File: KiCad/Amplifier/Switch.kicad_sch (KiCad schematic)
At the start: 49 parts, among them Q1 BD139, Q2 IXTH90P10P, Q4 BD139, Q5A1 BSC340N08NS3G, Q6 BD139, U1 AD8033

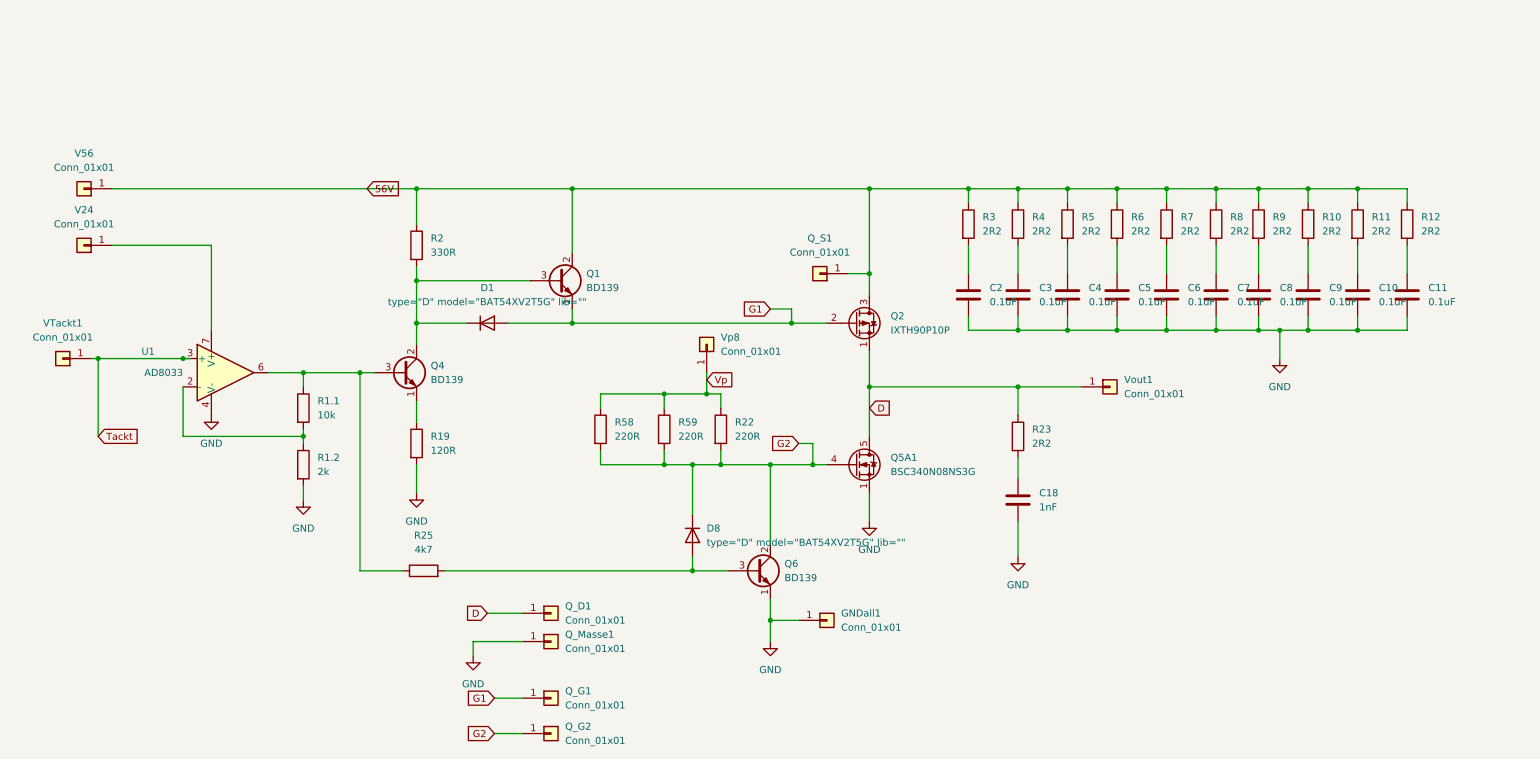
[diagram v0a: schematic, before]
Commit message: update Ampilfier
Schematic updated with separate pages.
all footprints added.
to do :
HF Part
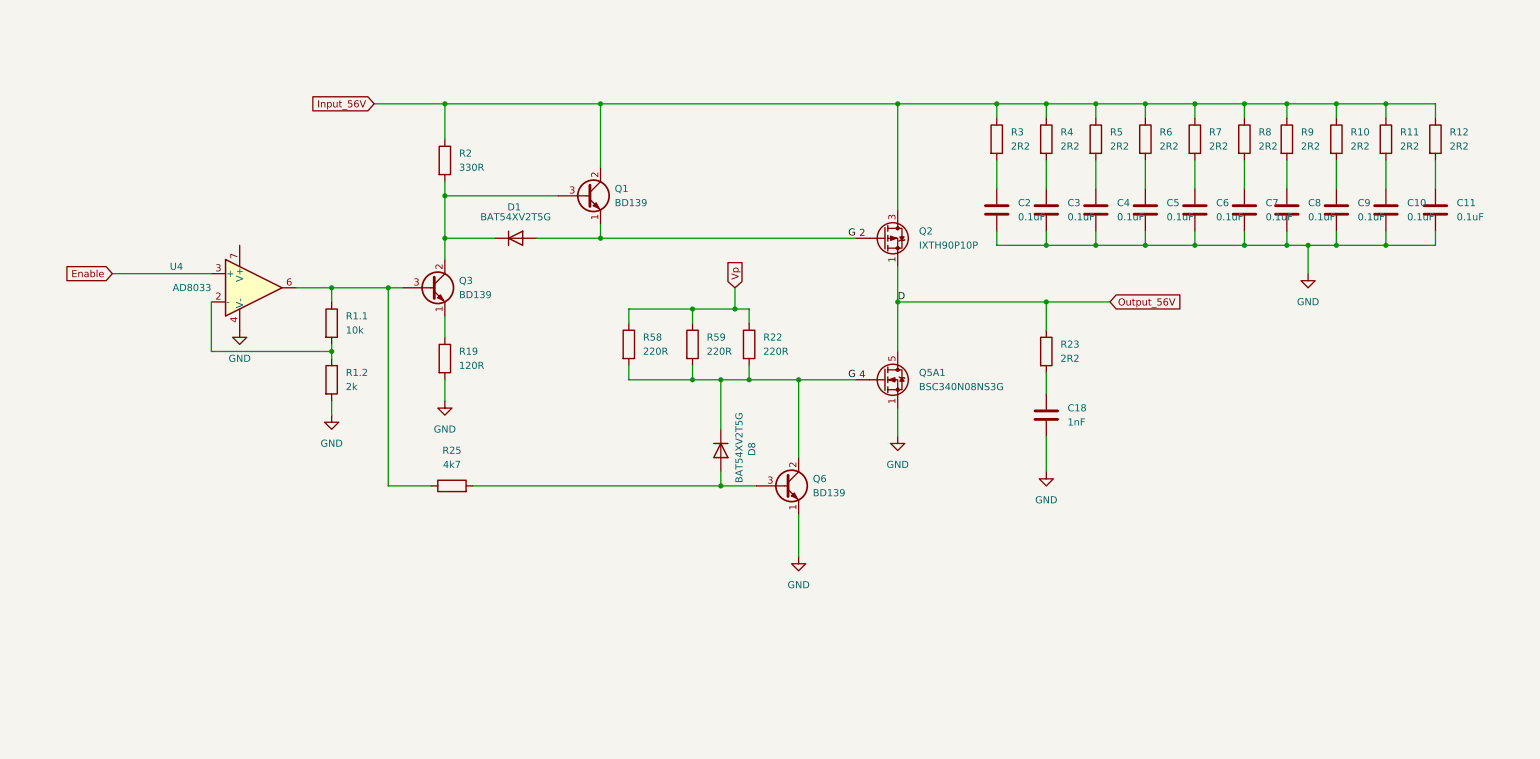
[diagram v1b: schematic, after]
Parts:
- removed GNDall1, V24, V56, VTackt1, Vout1, Vp8: Conn_01x01, Connector:Banana_Jack_1Pin, symbol Connector_Generic:Conn_01x01
- removed Q4: BD139, Package_TO_SOT_THT:TO-126-3_Vertical, symbol Transistor_BJT:BD139
- removed Q_D1, Q_G1, Q_G2, Q_Masse1, Q_S1: Conn_01x01, Connector_PinHeader_2.54mm:PinHeader_1x01_P2.54mm_Vertical, symbol Connector_Generic:Conn_01x01
- removed U1: AD8033, Package_SO:SOIC-8_3.9x4.9mm_P1.27mm, symbol Amplifier_Operational:AD8001AR
- added Q3: BD139, Package_TO_SOT_THT:TO-126-3_Vertical, symbol Transistor_BJT:BD139
- added U4: AD8033, Package_SO:SOIC-8_3.9x4.9mm_P1.27mm, symbol Amplifier_Operational:AD8001AR
- C10, C11, C18, C2, C3, C4, C5, C6, C7, C8, C9: footprint Capacitor_SMD:C_0805_2012Metric -> Capacitor_SMD:C_0603_1608Metric_Pad1.08x0.95mm_HandSolder
- D1, D8: value ${SIM.PARAMS} -> BAT54XV2T5G
- R1.1, R1.2, R23, R25: footprint Resistor_SMD:R_0805_2012Metric -> Resistor_SMD:R_0603_1608Metric_Pad0.98x0.95mm_HandSolder
- R10, R11, R12, R3, R4, R5, R6, R7, R8, R9: footprint Resistor_SMD:R_2512_6332Metric -> Resistor_SMD:R_0603_1608Metric_Pad0.98x0.95mm_HandSolder
- R19: footprint Resistor_SMD:R_1206_3216Metric -> Resistor_SMD:R_0603_1608Metric_Pad0.98x0.95mm_HandSolder
- R2, R22, R58, R59: footprint Resistor_SMD:R_1210_3225Metric -> Resistor_SMD:R_0603_1608Metric_Pad0.98x0.95mm_HandSolder
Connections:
- net G2 is gone; now on net G: D8.2 (K), Q5A1.4 (G), Q6.2 (C), R22.2, R58.2, R59.2
- net GND: now also U4.4 (V-)
- net at R19.1: now also Q3.1 (E)
- net at D1.2 (K), Q1.3 (B), R2.2: now also Q3.2 (C)
- net at R1.1.1, R25.1: now also Q3.3 (B), U4.6
- net at R1.1.2, R1.2.1: now also U4.2 (-)
- net 56V renamed Input_56V
- net D renamed Output_56V
- net G1 renamed G
- new net Enable: U4.3 (+)

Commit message: Platinenentwurf
die Platine wurde aufgebaut. Kontrolle fehlt
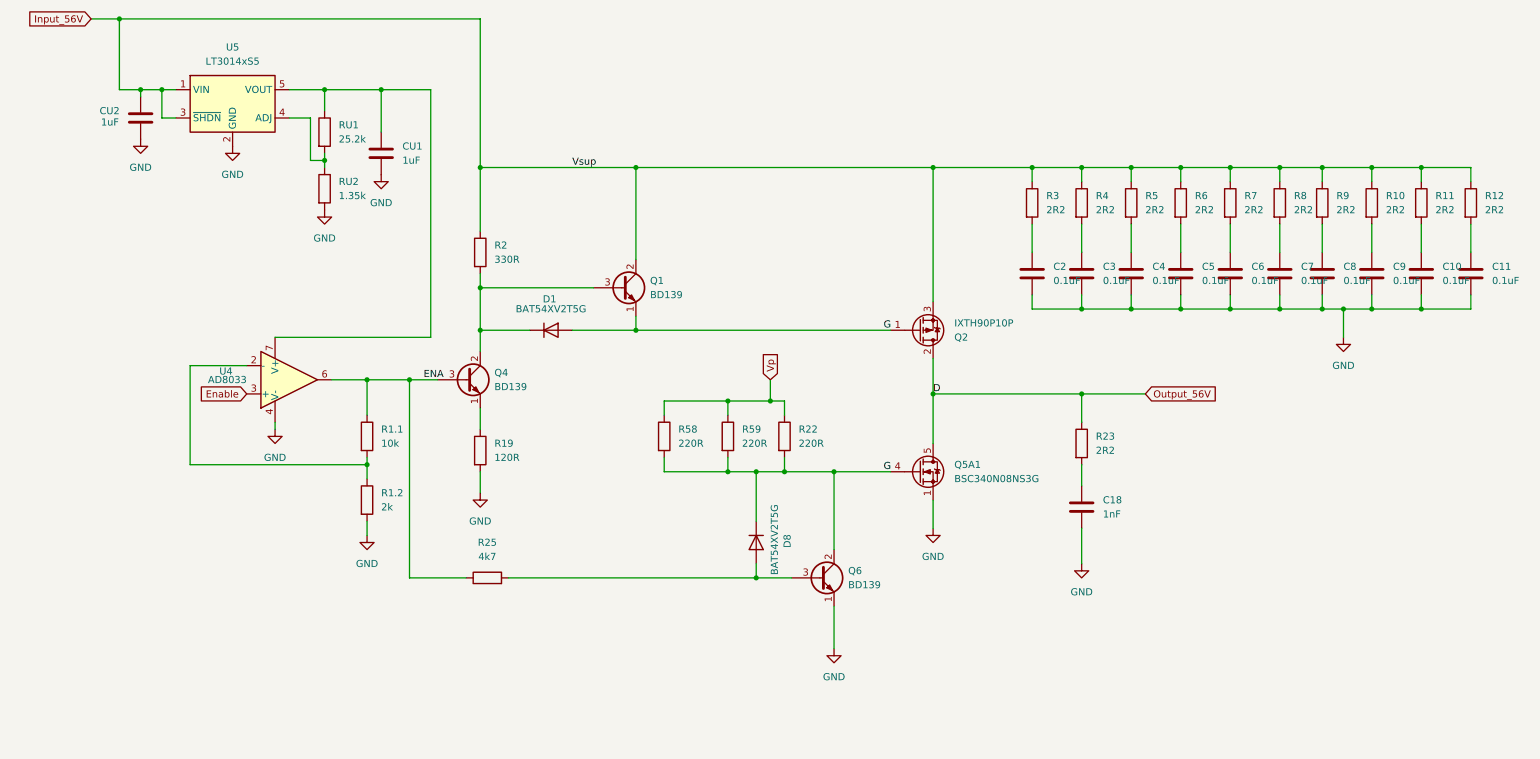
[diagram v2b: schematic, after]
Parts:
- added CU1, CU2: 1uF, Capacitor_SMD:C_0603_1608Metric_Pad1.08x0.95mm_HandSolder, symbol Device:C
- added RU1: 25.2k, Resistor_SMD:R_0603_1608Metric_Pad0.98x0.95mm_HandSolder, symbol Device:R
- added RU2: 1.35k, Resistor_SMD:R_0603_1608Metric_Pad0.98x0.95mm_HandSolder, symbol Device:R
- added U5: LT3014xS5, Package_TO_SOT_SMD:SOT-23-5, symbol Regulator_Linear:LT3014xS5
- R10, R11, R12, R3, R4, R5, R6, R7, R8, R9: footprint Resistor_SMD:R_0603_1608Metric_Pad0.98x0.95mm_HandSolder -> Resistor_SMD:R_2512_6332Metric_Pad1.40x3.35mm_HandSolder
- renumbered Q3 to Q4
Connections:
- net G: now also Q2.1 (G); no longer Q2.2 (G)
- net GND: now also CU1.2, CU2.2, RU2.2, U5.2 (GND)
- net Input_56V: now also CU2.1, U5.1 (VIN), U5.3 (~{SHDN})
- net Output_56V: now also Q2.2 (D); no longer Q2.1 (S)
- net ENA: now reaches Q4.3 (B), R1.1.1, R25.1, U4.6
- net at U4.7 (V+): now also CU1.1, RU1.1, U5.5 (VOUT)
- new net: RU1.2, RU2.1, U5.4 (ADJ)
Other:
- moved on the sheet: C10, C11, C18, C2, C3, C4, C5, C6, C7, C8, C9, D1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
